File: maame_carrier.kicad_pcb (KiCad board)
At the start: 2 copper layers, 95 x 95 mm, 25 parts, among them J1 To Kakute: left strip R3 G 5V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, J10 FS-iA10B iBUS servo lead (S +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, J11 TF-Luna pin order 1-6 (CFG ti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, J12 Spare FC I2C (5 V supply, sha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, J13 Payload servo on M5 (S + -), J14 Spare output M6 (S + -), J15 Spare output M7 (S + -), J16 Spare output M8 (S + -), J2 To Kakute 8-pin port 2 leads: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, J3 VBAT tap from ESC battery pad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, J4 Micro BEC input leads, J5 Micro BEC output leads (set t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, J6 Spare power: 5V_AUX G 5V_FC G, J7 Pi expansion: 3V3 logic ONLY, J8 TBS M10Q: order matches its p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, J9 SiK radio (UART4), U1 Raspberry Pi Zero W v1.1, com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

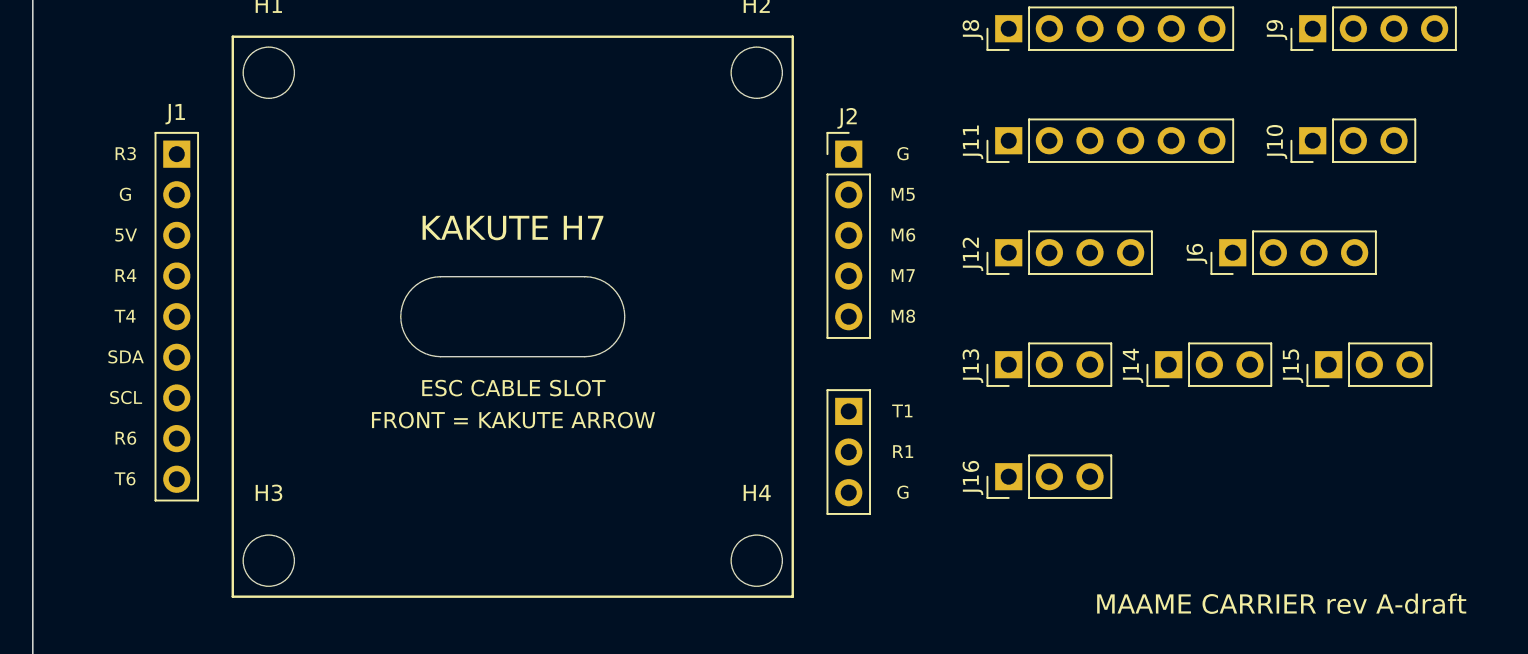
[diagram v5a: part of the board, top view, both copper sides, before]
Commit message: J1 mirrors the full Kakute V1.5 left strip (2x9, B+ unwired) + T1/R1/G; drop M5-M8 (J2, J14-J16); J13 -> servo power; add J17 Kakute spare (T3, RSSI, 3V3)
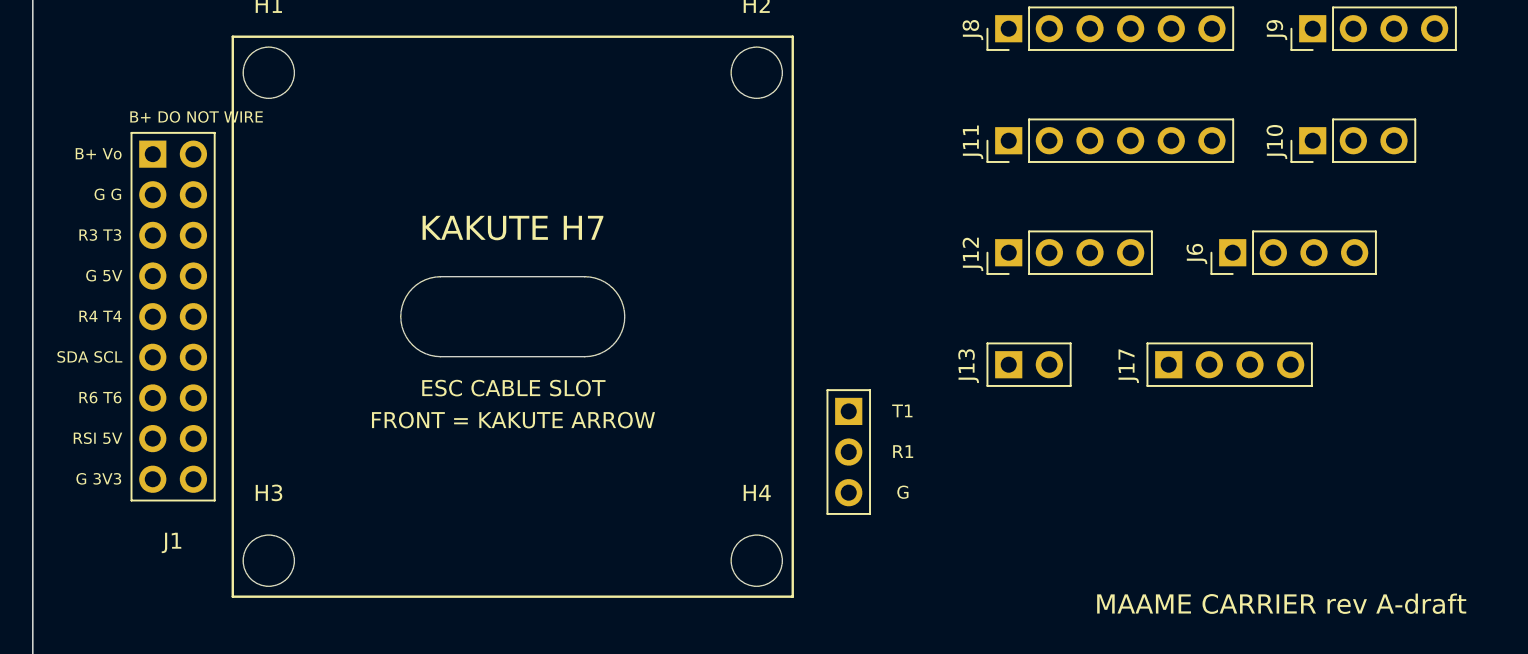
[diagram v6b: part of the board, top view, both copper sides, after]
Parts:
- removed J14: Spare output M6 (S + -), Connector_PinHeader_2.54mm:PinHeader_1x03_P2.54mm_Vertical
- removed J15: Spare output M7 (S + -), Connector_PinHeader_2.54mm:PinHeader_1x03_P2.54mm_Vertical
- removed J16: Spare output M8 (S + -), Connector_PinHeader_2.54mm:PinHeader_1x03_P2.54mm_Vertical
- removed J2: To Kakute 8-pin port 2 leads: GND M5 M6, Connector_PinHeader_2.54mm:PinHeader_1x05_P2.54mm_Vertical
- added J17: Kakute spare: T3 RSSI 3V3(FC) G, Connector_PinHeader_2.54mm:PinHeader_1x04_P2.54mm_Vertical, F.Cu at (71.0, 25.0)
- J1: value To Kakute: left strip R3 G 5V R4 T4 SDA SCL R6 T6, JST T1 R1 G -> To Kakute H7 V1.5: full left pad strip 2x9 (B+ not wired) + JST T1 R1 G; footprint maame_carrier:Kakute_Pads_L9_R3 -> maame_carrier:Kakute_Pads_2x9_R3
- J13: value Payload servo on M5 (S + -) -> Payload servo power (+ -); servo signal plugs into the Kakute port-2 lead; footprint Connector_PinHeader_2.54mm:PinHeader_1x03_P2.54mm_Vertical -> Connector_PinHeader_2.54mm:PinHeader_1x02_P2.54mm_Vertical
- moved J1 1.50 mm to (7.50, 11.8)
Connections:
- J1 pad 1: RC_IBUS -> (no net)
- J1 pad 10: UART1_FC_TX -> UART4_FC_TX
- J1 pad 11: UART1_FC_RX -> I2C_SDA
- J1 pad 12: GND -> I2C_SCL
- J1 pad 2: GND -> (no net)
- J1 pad 3: 5V_FC -> GND
- J1 pad 4: UART4_FC_RX -> GND
- J1 pad 5: UART4_FC_TX -> RC_IBUS
- J1 pad 6: I2C_SDA -> UART3_TX_SPARE
- J1 pad 7: I2C_SCL -> GND
- J1 pad 8: UART6_FC_RX -> 5V_FC
- J1 pad 9: UART6_FC_TX -> UART4_FC_RX
- J13 pad 1: OUT5 -> 5V_AUX
- J13 pad 2: 5V_AUX -> GND
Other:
- board text removed: "G"
- board text removed: "M5"
- board text removed: "M6"
- board text removed: "M7"
- board text removed: "M8"

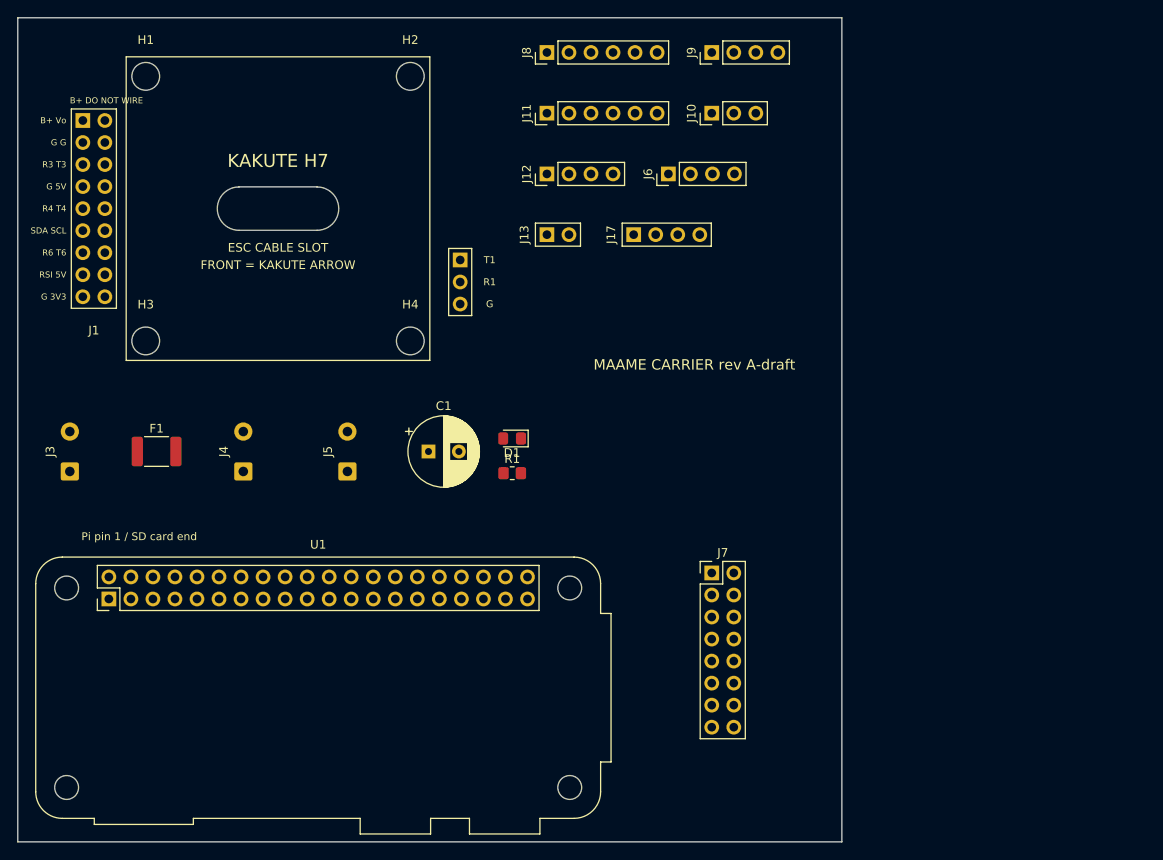
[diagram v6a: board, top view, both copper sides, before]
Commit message: Silkscreen pass: every pin named, connector titles, pin-1 dots, polarity, rails, nose arrow, Pi orientation, board id; headers vertical
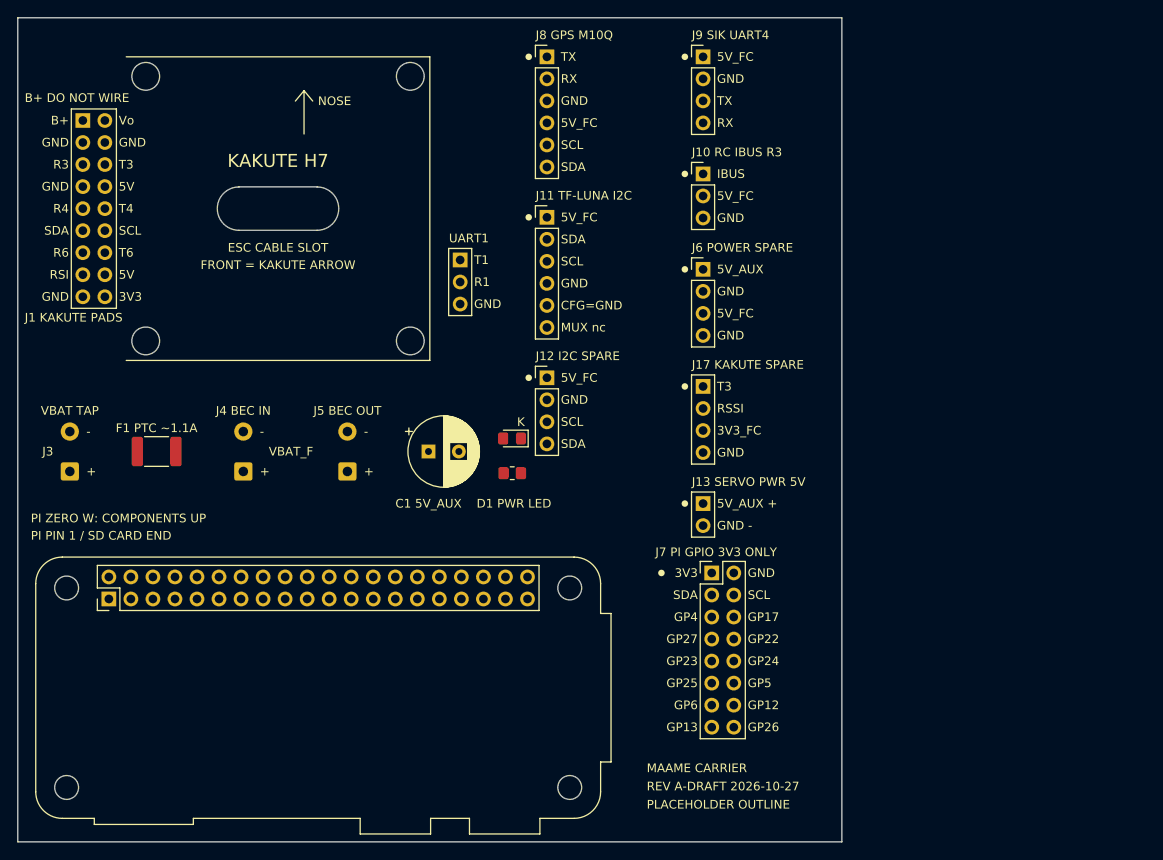
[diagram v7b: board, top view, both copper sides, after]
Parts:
- moved J13 35.8 mm to (79.0, 56.0), turned to 0 degrees
- moved J12 23.5 mm to (61.0, 41.5), turned to 0 degrees
- moved J17 19.2 mm to (79.0, 42.5), turned to 0 degrees
- moved J11 12.0 mm to (61.0, 23.0), turned to 0 degrees
- moved J6 11.7 mm to (79.0, 29.0), turned to 0 degrees
- moved J10 7.07 mm to (79.0, 18.0), turned to 0 degrees
- moved J9 1.12 mm to (79.0, 4.50), turned to 0 degrees
- moved J8 0.50 mm to (61.0, 4.50), turned to 0 degrees
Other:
- board text added: "+"
- board text added: "-"
- board text added: "3V3"
- board text added: "3V3_FC"
- board text added: "5V"
- board text added: "5V_AUX"
- board text added: "5V_AUX +"
- board text added: "5V_FC"
- board text added: "B+"
- board text added: "B+ DO NOT WIRE"
- board text added: "C1 5V_AUX"
- board text added: "CFG=GND"
- board text added: "D1 PWR LED"
- board text added: "F1 PTC ~1.1A"
- board text added: "GND"
- board text added: "GND -"
- board text added: "GP12"
- board text added: "GP13"
- board text added: "GP17"
- board text added: "GP22"
- board text added: "GP23"
- board text added: "GP24"
- board text added: "GP25"
- board text added: "GP26"
- board text added: "GP27"
- board text added: "GP4"
- board text added: "GP5"
- board text added: "GP6"
- board text added: "IBUS"
- board text added: "J1 KAKUTE PADS"
- board text added: "J10 RC IBUS R3"
- board text added: "J11 TF-LUNA I2C"
- board text added: "J12 I2C SPARE"
- board text added: "J13 SERVO PWR 5V"
- board text added: "J17 KAKUTE SPARE"
- board text added: "J3"
- board text added: "J4 BEC IN"
- board text added: "J5 BEC OUT"
- board text added: "J6 POWER SPARE"
- board text added: "J7 PI GPIO 3V3 ONLY"
- board text added: "J8 GPS M10Q"
- board text added: "J9 SIK UART4"
- board text added: "K"
- board text added: "MAAME CARRIER"
- board text added: "MUX nc"
- board text added: "NOSE"
- board text added: "PI PIN 1 / SD CARD END"
- board text added: "PI ZERO W: COMPONENTS UP"
- board text added: "PLACEHOLDER OUTLINE"
- board text added: "R1"
- board text added: "R3"
- board text added: "R4"
- board text added: "R6"
- board text added: "REV A-DRAFT 2026-10-27"
- board text added: "RSI"
- board text added: "RSSI"
- board text added: "RX"
- board text added: "SCL"
- board text added: "SDA"
- board text added: "T1"
- board text added: "T3"
- board text added: "T4"
- board text added: "T6"
- board text added: "TX"
- board text added: "UART1"
- board text added: "VBAT TAP"
- board text added: "VBAT_F"
- board text added: "Vo"
- board text removed: "MAAME CARRIER rev A-draft"
- board text removed: "Pi pin 1 / SD card end"

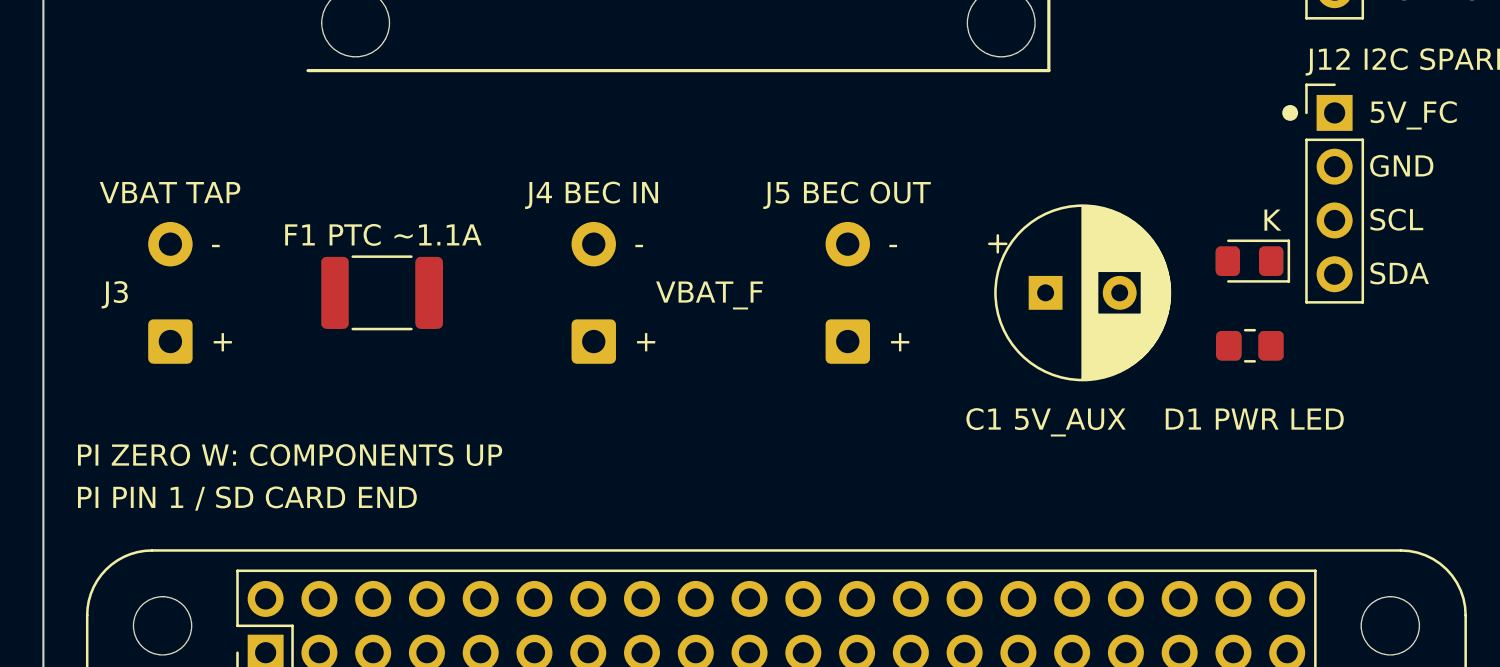
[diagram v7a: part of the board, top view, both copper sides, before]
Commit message: Reserve 18x15 mm micro BEC box between J4/J5 (no reverse protection warning); re-space power row; BEC schematic note
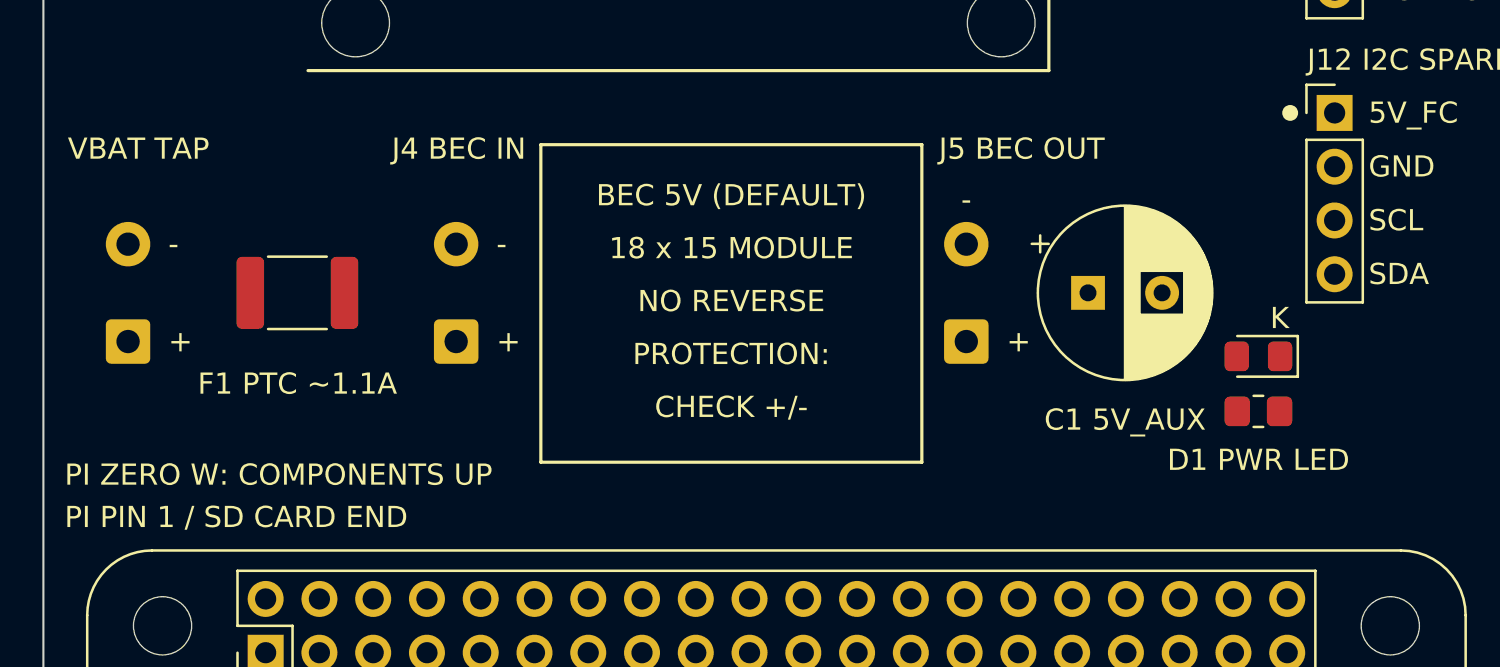
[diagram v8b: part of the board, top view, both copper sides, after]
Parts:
- J4: value Micro BEC input leads -> Micro BEC input leads (6-60 V, NO reverse protection)
- moved J4 6.50 mm to (19.5, 52.3)
- moved J5 5.60 mm to (43.6, 52.3)
- moved D1 4.52 mm to (57.4, 53.0)
- moved F1 4.00 mm to (12.0, 50.0)
- moved R1 3.13 mm to (57.4, 55.6)
- moved C1 2.00 mm to (49.4, 50.0)
- moved J3 2.00 mm to (4.00, 52.3)
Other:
- board text added: "18 x 15 MODULE"
- board text added: "BEC 5V (DEFAULT)"
- board text added: "CHECK +/-"
- board text added: "NO REVERSE"
- board text added: "PROTECTION:"
- board text removed: "J3"
- board text removed: "VBAT_F"
